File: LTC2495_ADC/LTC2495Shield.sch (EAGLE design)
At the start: 5 parts

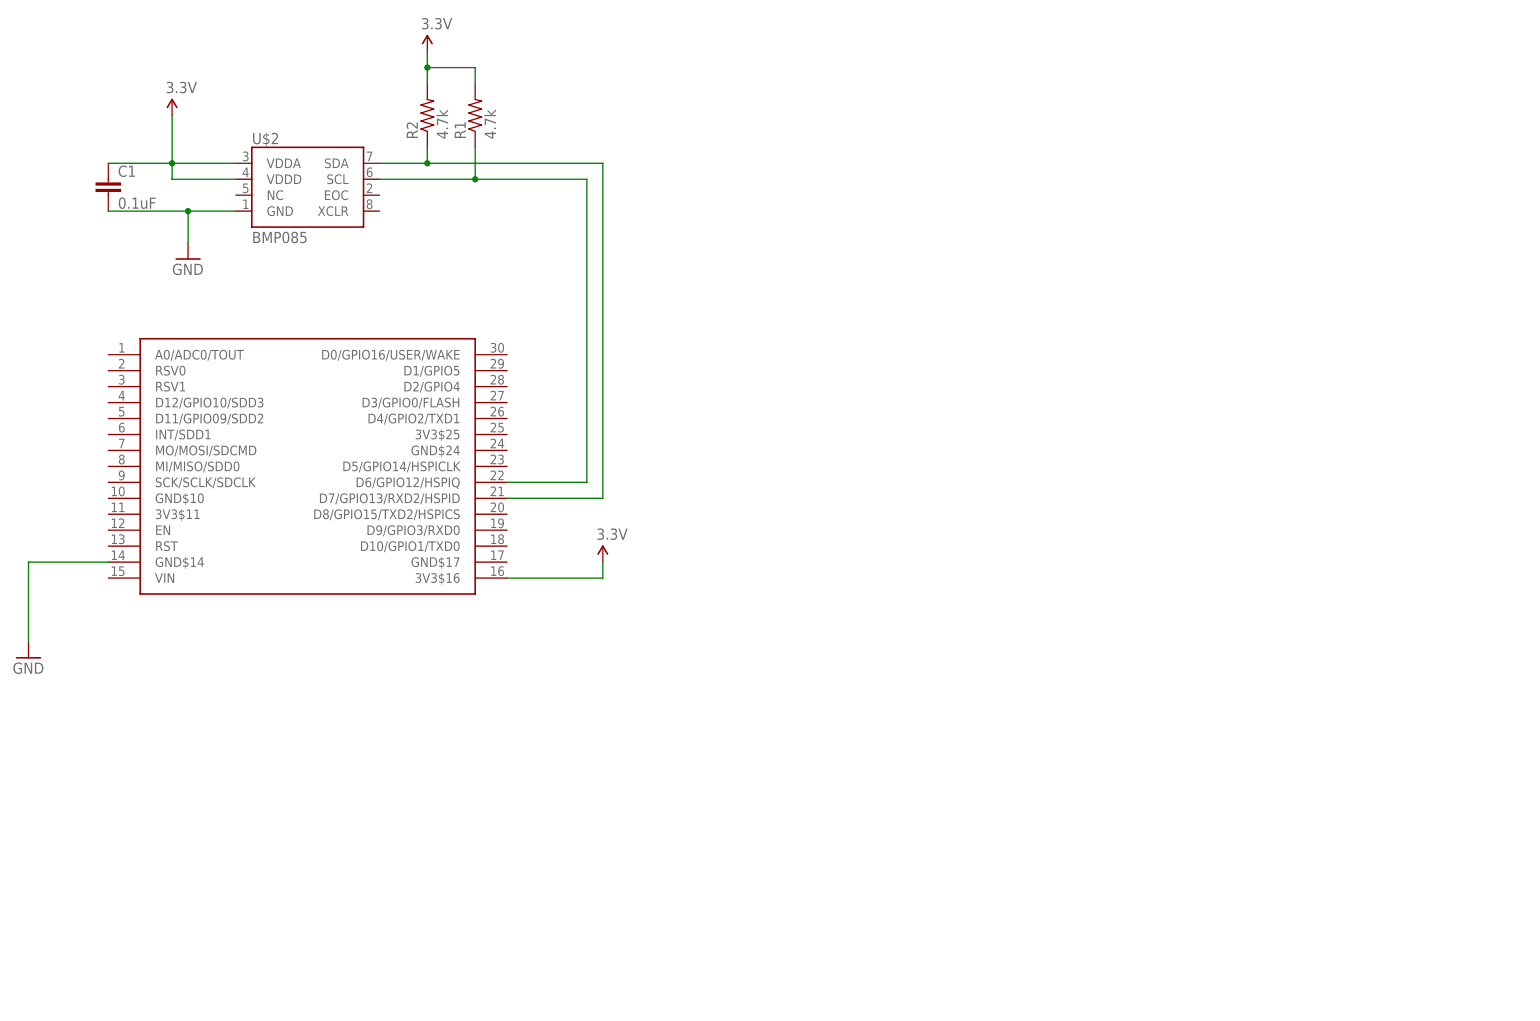
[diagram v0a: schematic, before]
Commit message: Updated BMP180 symbol Removed BMP085 shield (redundant) Added DS3231 RTC Shield Added LTC2495 ADC Shield Added chip data sheets for each shield
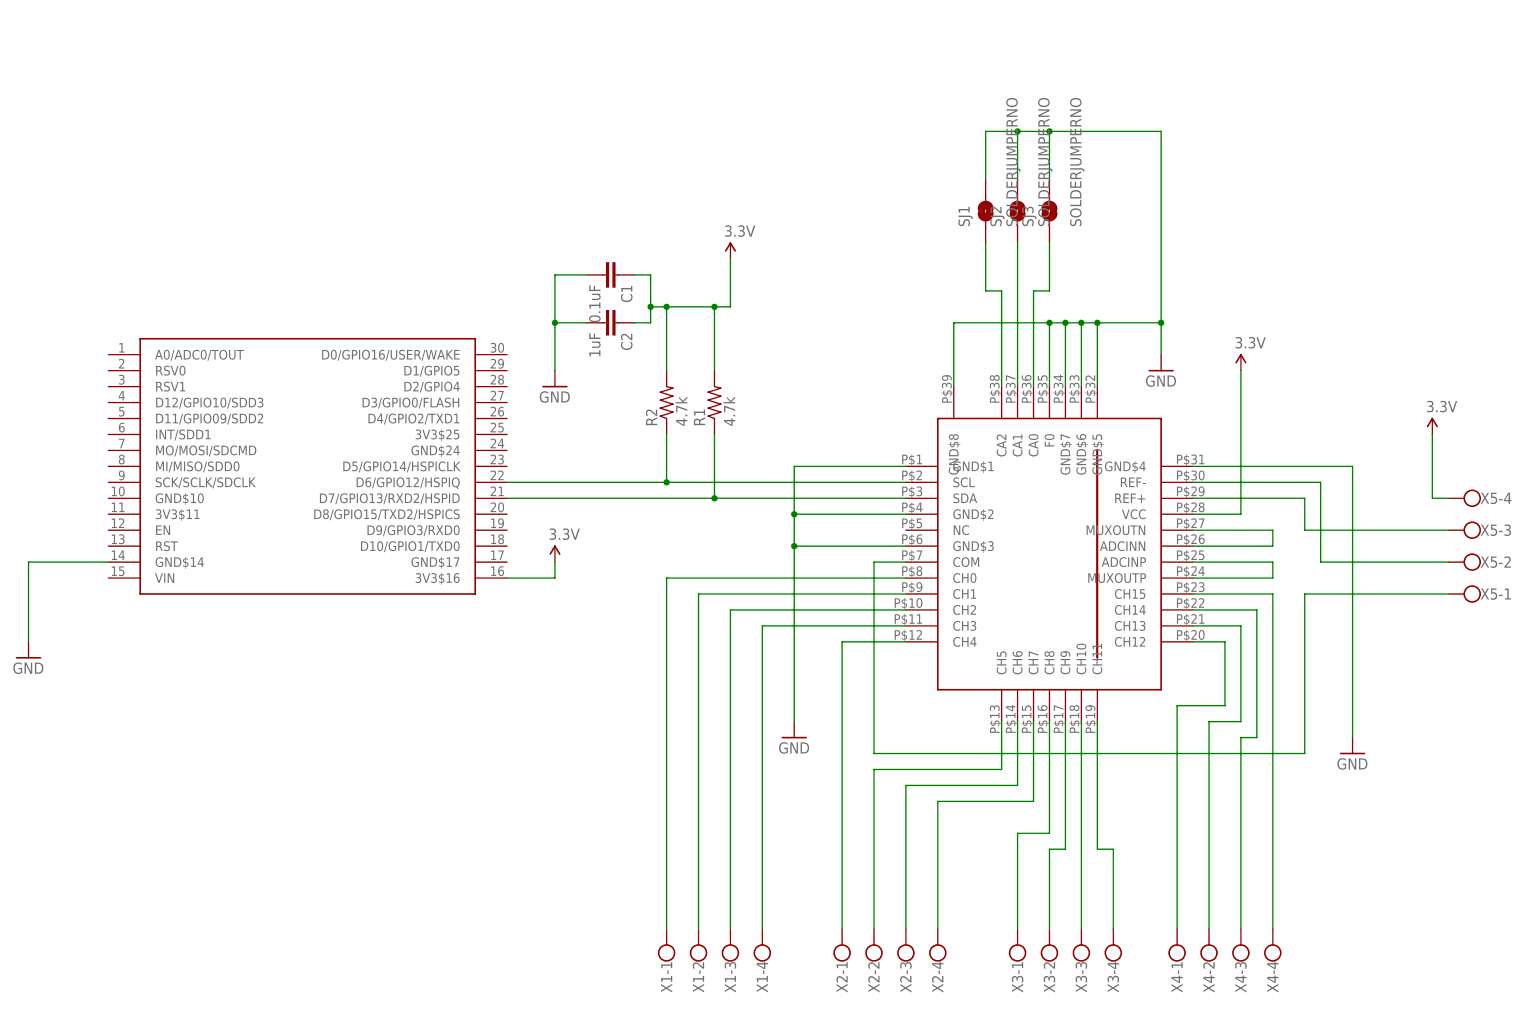
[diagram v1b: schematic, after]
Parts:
- removed U$2: BMP085, SparkFun:BMP085
- added C2: 1uF, SparkFun:CAP0402-CAP
- added SJ1, SJ2, SJ3: SOLDERJUMPERNO, SparkFun:SOLDERJUMPERNO
- added U$3: LTC2495, SparkFun-AnalogIC:LTC2495
- added X1, X2, X3, X4, X5: (no value), con-wago-500:W237-4
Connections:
- new net N$10: U$3.CH6, X2-3.KL
- new net N$11: U$3.CH7, X2-4.KL
- new net N$12: U$3.CH8, X3-1.KL
- new net N$13: U$3.CH9, X3-2.KL
- new net N$14: U$3.CH10, X3-3.KL
- new net N$15: U$3.CH11, X3-4.KL
- new net N$16: U$3.CH12, X4-1.KL
- new net N$17: U$3.CH13, X4-2.KL
- new net N$18: U$3.CH14, X4-3.KL
- new net N$19: U$3.CH15, X4-4.KL
- new net N$20: SJ1.1, U$3.CA2
- new net N$21: SJ2.1, U$3.CA1
- new net N$22: SJ3.1, U$3.CA0
- new net N$25: U$3.COM, X5-1.KL
- new net N$26: U$3.REF+, X5-3.KL
- new net N$27: U$3.REF-, X5-2.KL
- new net N$28: U$3.ADCINN, U$3.MUXOUTN
- new net N$29: U$3.ADCINP, U$3.MUXOUTP
- new net N$4: U$3.CH1, X1-2.KL
- new net N$5: U$3.CH2, X1-3.KL
- new net N$6: U$3.CH3, X1-4.KL
- new net N$7: U$3.CH4, X2-1.KL
- new net N$8: R2.1, U$1.D6/GPIO12/HSPIQ, U$3.SCL
- new net N$9: U$3.CH5, X2-2.KL
- net 3.3V: now also C2.1, U$3.VCC, X5-4.KL; no longer U$2.VDDA, U$2.VDDD
- net GND: now also C2.2, SJ1.2, SJ2.2, SJ3.2, U$3.F0, U$3.GND$1, U$3.GND$2, U$3.GND$3, U$3.GND$4, U$3.GND$5, U$3.GND$6, U$3.GND$7, U$3.GND$8; no longer U$2.GND
- net N$2: now also R1.1, U$3.SDA; no longer R2.1, U$2.SDA
- net N$3: now also U$3.CH0, X1-1.KL; no longer R1.1, U$1.D6/GPIO12/HSPIQ, U$2.SCL
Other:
- moved on the sheet: C1, R1, R2
